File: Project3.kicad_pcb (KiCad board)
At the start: 2 copper layers, 7 parts, among them SW1 SW_Push_Open

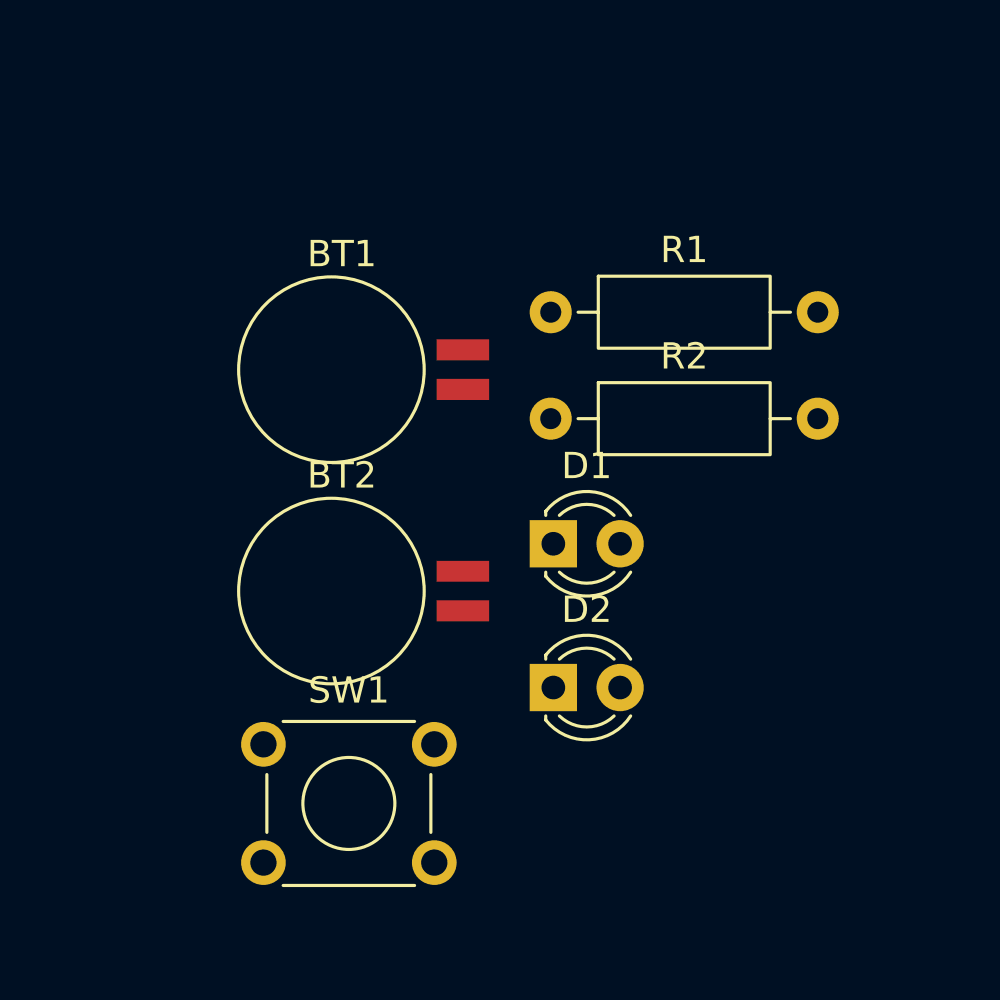
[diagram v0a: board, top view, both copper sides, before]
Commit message: Component placement is done
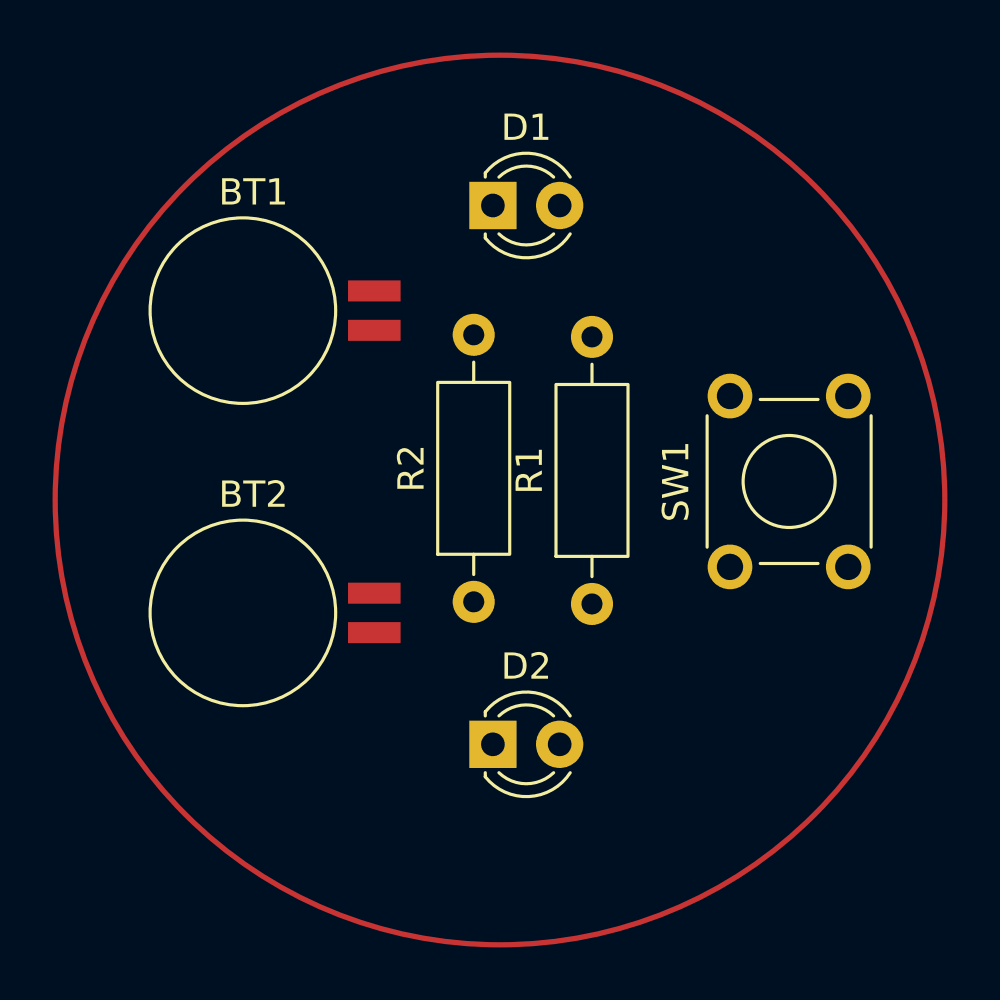
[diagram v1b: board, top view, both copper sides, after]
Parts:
- moved SW1 19.0 mm to (141.2, 85.2), turned to 90 degrees
- moved D1 13.1 mm to (132.2, 71.5)
- moved R1 11.2 mm to (136.0, 86.7), turned to 90 degrees
- moved R2 7.56 mm to (131.5, 86.6), turned to 90 degrees
- moved BT1 4.05 mm to (127.7, 75.5)
- moved BT2 3.47 mm to (127.7, 87.0)
- moved D2 3.16 mm to (132.2, 92.0)
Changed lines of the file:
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@@
 	(footprint "Resistor_THT:R_Axial_DIN0207_L6.3mm_D2.5mm_P10.16mm_Horizontal"
 		(layer "F.Cu")
-		(at 134.43 75.56)
+		(at 136 86.66 90)
 		(descr "Resistor, Axial_DIN0207 series, Axial, Horizontal, pin pitch=10.16mm, 0.25W = 1/4W, length*diameter=6.3*2.5mm^2, http://cdn-reichelt.de/documents/datenblatt/B400/1_4W%23YAG.pdf")
 		(tags "Resistor Axial_DIN0207 series Axial Horizontal pin pitch 10.16mm 0.25W = 1/4W length 6.3mm diameter 2.5mm")
 		(property "Reference" "R1"
-			(at 5.08 -2.37 0)
+			(at 5.08 -2.37 90)
 			(layer "F.SilkS")
 			(effects
@@
 		)
 		(property "Value" "R"
-			(at 5.08 2.37 0)
+			(at 5.08 2.37 90)
 			(layer "F.Fab")
 			(effects
@@
 		)
 		(property "Datasheet" "~"
-			(at 0 0 0)
+			(at 0 0 90)
 			(layer "F.Fab")
 			(hide yes)
@@
 		)
 		(property "Description" "Resistor"
-			(at 0 0 0)
+			(at 0 0 90)
 			(layer "F.Fab")
 			(hide yes)
@@
 		(attr through_hole)
 		(fp_line
+			(start 9.12 0)
+			(end 8.35 0)
+			(stroke
+				(width 0.12)
+				(type solid)
+			)
+			(layer "F.SilkS")
+		)
+		(fp_line
 			(start 1.04 0)
 			(end 1.81 0)
-			(stroke
-				(width 0.12)
-				(type solid)
-			)
-			(layer "F.SilkS")
-		)
-		(fp_line
-			(start 9.12 0)
-			(end 8.35 0)
 			(stroke
 				(width 0.12)
@@
 		)
 		(fp_line
+			(start 10.16 0)
+			(end 8.23 0)
+			(stroke
+				(width 0.1)
+				(type solid)
+			)
+			(layer "F.Fab")
+		)
+		(fp_line
 			(start 0 0)
 			(end 1.93 0)
-			(stroke
-				(width 0.1)
-				(type solid)
-			)
-			(layer "F.Fab")
-		)
-		(fp_line
-			(start 10.16 0)
-			(end 8.23 0)
 			(stroke
 				(width 0.1)
@@
 		)
 		(fp_text user "${REFERENCE}"
-			(at 5.08 0 0)
+			(at 5.08 0 90)
 			(layer "F.Fab")
 			(effects
@@
 		)
 		(pad "1" thru_hole circle
-			(at 0 0)
+			(at 0 0 90)
 			(size 1.6 1.6)
 			(drill 0.8)
@@
 		)
 		(pad "2" thru_hole circle
-			(at 10.16 0)
+			(at 10.16 0 90)
 			(size 1.6 1.6)
 			(drill 0.8)
@@
 	(footprint "Battery:BatteryHolder_Seiko_MS621F"
 		(layer "F.Cu")
-		(at 131.086204 86.168612)
+		(at 127.718102 87)
 		(descr "Seiko MS621F, https://www.sii.co.jp/en/me/files/2014/02/file_EXTENDED_PRDCT_SPEC_75_FILE_11.jpg")
 		(tags "Seiko MS621F")
 		(property "Reference" "BT2"
-			(at -4.6 -4.4 0)
+			(at -4.6 -4.5 0)
 			(layer "F.SilkS")
 			(effects
@@
 		)
 		(fp_text user "${REFERENCE}"
-			(at 0 0 0)
+			(at 0 -0.1 0)
 			(layer "F.Fab")
 			(effects
@@
 	(footprint "LED_THT:LED_D3.0mm"
 		(layer "F.Cu")
-		(at 134.53 89.84)
+		(at 132.23 92)
 		(descr "LED, diameter 3.0mm, 2 pins, generated by kicad-footprint-generator")
 		(tags "LED")
@@
 	(footprint "Battery:BatteryHolder_Seiko_MS621F"
 		(layer "F.Cu")
-		(at 131.086204 77.746204)
+		(at 127.718102 75.5)
 		(descr "Seiko MS621F, https://www.sii.co.jp/en/me/files/2014/02/file_EXTENDED_PRDCT_SPEC_75_FILE_11.jpg")
 		(tags "Seiko MS621F")
 		(property "Reference" "BT1"
-			(at -4.6 -4.4 0)
+			(at -4.6 -4.5 0)
 			(layer "F.SilkS")
 			(effects
@@
 		)
 		(fp_text user "${REFERENCE}"
-			(at 0 0 0)
+			(at 0 -0.1 0)
 			(layer "F.Fab")
 			(effects
@@
 	(footprint "LED_THT:LED_D3.0mm"
 		(layer "F.Cu")
-		(at 134.53 84.37)
+		(at 132.23 71.5)
 		(descr "LED, diameter 3.0mm, 2 pins, generated by kicad-footprint-generator")
 		(tags "LED")
@@
 		)
 		(property "Value" "LED"
-			(at 1.27 2.96 0)
+			(at 4.27 3.96 0)
 			(layer "F.Fab")
 			(effects
@@
 	(footprint "Resistor_THT:R_Axial_DIN0207_L6.3mm_D2.5mm_P10.16mm_Horizontal"
 		(layer "F.Cu")
-		(at 134.43 79.61)
+		(at 131.5 86.58 90)
 		(descr "Resistor, Axial_DIN0207 series, Axial, Horizontal, pin pitch=10.16mm, 0.25W = 1/4W, length*diameter=6.3*2.5mm^2, http://cdn-reichelt.de/documents/datenblatt/B400/1_4W%23YAG.pdf")
 		(tags "Resistor Axial_DIN0207 series Axial Horizontal pin pitch 10.16mm 0.25W = 1/4W length 6.3mm diameter 2.5mm")
 		(property "Reference" "R2"
-			(at 5.08 -2.37 0)
+			(at 5.08 -2.37 90)
 			(layer "F.SilkS")
 			(effects
@@
 		)
 		(property "Value" "R"
-			(at 5.08 2.37 0)
+			(at 5.08 2.37 90)
 			(layer "F.Fab")
 			(effects
@@
 		)
 		(property "Datasheet" "~"
-			(at 0 0 0)
+			(at 0 0 90)
 			(layer "F.Fab")
 			(hide yes)
@@
 		)
 		(property "Description" "Resistor"
-			(at 0 0 0)
+			(at 0 0 90)
 			(layer "F.Fab")
 			(hide yes)
@@
 		(attr through_hole)
 		(fp_line
+			(start 9.12 0)
+			(end 8.35 0)
+			(stroke
+				(width 0.12)
+				(type solid)
+			)
+			(layer "F.SilkS")
+		)
+		(fp_line
 			(start 1.04 0)
 			(end 1.81 0)
-			(stroke
-				(width 0.12)
-				(type solid)
-			)
-			(layer "F.SilkS")
-		)
-		(fp_line
-			(start 9.12 0)
-			(end 8.35 0)
 			(stroke
 				(width 0.12)
@@
 		)
 		(fp_line
+			(start 10.16 0)
+			(end 8.23 0)
+			(stroke
+				(width 0.1)
+				(type solid)
+			)
+			(layer "F.Fab")
+		)
+		(fp_line
 			(start 0 0)
 			(end 1.93 0)
-			(stroke
-				(width 0.1)
-				(type solid)
-			)
-			(layer "F.Fab")
-		)
-		(fp_line
-			(start 10.16 0)
-			(end 8.23 0)
 			(stroke
 				(width 0.1)
@@
 		)
 		(fp_text user "${REFERENCE}"
-			(at 5.08 0 0)
+			(at 5.08 0 90)
 			(layer "F.Fab")
 			(effects
@@
 		)
 		(pad "1" thru_hole circle
-			(at 0 0)
+			(at 0 0 90)
 			(size 1.6 1.6)
 			(drill 0.8)
@@
 		)
 		(pad "2" thru_hole circle
-			(at 10.16 0)
+			(at 10.16 0 90)
 			(size 1.6 1.6)
 			(drill 0.8)
@@
 	(footprint "Button_Switch_THT:SW_TH_Tactile_Omron_B3F-106x"
 		(layer "F.Cu")
-		(at 123.5 92)
+		(at 141.25 85.25 90)
 		(descr "Tactile switch, 6x6 mm, H7.0 mm, 6.5 mm pitch, https://omronfs.omron.com/en_US/ecb/products/pdf/en-b3f.pdf")
 		(tags "Omron B3F-10xx SPST 1P1T")
 		(property "Reference" "SW1"
-			(at 3.25 -2.05 0)
+			(at 3.25 -2.05 90)
 			(layer "F.SilkS")
 			(effects
@@
 		)
 		(property "Value" "SW_Push_Open"
-			(at 3.25 6.5 0)
+			(at 3.25 6.5 90)
 			(layer "F.Fab")
 			(effects
@@
 		)
 		(property "Datasheet" "~"
-			(at 0 0 0)
+			(at 0 0 90)
 			(unlocked yes)
 			(layer "F.Fab")
@@
 		)
 		(property "Description" "Push button switch, push-to-open, generic, two pins"
-			(at 0 0 0)
+			(at 0 0 90)
 			(unlocked yes)
 			(layer "F.Fab")
@@
 		(attr through_hole)
 		(fp_line
+			(start 0.75 -0.87)
+			(end 5.75 -0.87)
+			(stroke
+				(width 0.12)
+				(type solid)
+			)
+			(layer "F.SilkS")
+		)
+		(fp_line
+			(start 6.37 1.15)
+			(end 6.37 3.35)
+			(stroke
+				(width 0.12)
+				(type solid)
+			)
+			(layer "F.SilkS")
+		)
+		(fp_line
 			(start 0.13 3.35)
 			(end 0.13 1.15)
@@
 		)
 		(fp_line
-			(start 0.75 -0.87)
-			(end 5.75 -0.87)
-			(stroke
-				(width 0.12)
-				(type solid)
-			)
-			(layer "F.SilkS")
-		)
-		(fp_line
 			(start 0.75 5.37)
 			(end 5.75 5.37)
-			(stroke
-				(width 0.12)
-				(type solid)
-			)
-			(layer "F.SilkS")
-		)
-		(fp_line
-			(start 6.37 1.15)
-			(end 6.37 3.35)
 			(stroke
 				(width 0.12)
@@
 		(fp_line
 			(start -1.1 -1.1)
+			(end 7.6 -1.1)
+			(stroke
+				(width 0.05)
+				(type solid)
+			)
+			(layer "F.CrtYd")
+		)
+		(fp_line
+			(start -1.1 -1.1)
 			(end -1.1 5.6)
 			(stroke
@@
 		)
 		(fp_line
-			(start -1.1 -1.1)
+			(start 7.6 5.6)
 			(end 7.6 -1.1)
 			(stroke
@@
 		)
 		(fp_line
-			(start 7.6 5.6)
-			(end 7.6 -1.1)
-			(stroke
-				(width 0.05)
-				(type solid)
-			)
-			(layer "F.CrtYd")
+			(start 6.25 -0.75)
+			(end 6.25 5.25)
+			(stroke
+				(width 0.1)
+				(type solid)
+			)
+			(layer "F.Fab")
+		)
+		(fp_line
+			(start 0.25 -0.75)
+			(end 6.25 -0.75)
+			(stroke
+				(width 0.1)
+				(type solid)
+			)
+			(layer "F.Fab")
 		)
 		(fp_line
@@
 		)
 		(fp_line
-			(start 0.25 -0.75)
-			(end 6.25 -0.75)
-			(stroke
-				(width 0.1)
-				(type solid)
-			)
-			(layer "F.Fab")
-		)
-		(fp_line
 			(start 0.25 5.25)
 			(end 6.25 5.25)
@@
 			(layer "F.Fab")
 		)
-		(fp_line
-			(start 6.25 -0.75)
-			(end 6.25 5.25)
-			(stroke
-				(width 0.1)
-				(type solid)
-			)
-			(layer "F.Fab")
-		)
 		(fp_text user "${REFERENCE}"
-			(at 3.25 2.25 0)
+			(at 3.25 2.25 90)
 			(layer "F.Fab")
 			(effects
@@
 		)
 		(pad "1" thru_hole circle
-			(at 0 0)
+			(at 0 0 90)
 			(size 1.7 1.7)
 			(drill 1)
@@
 		)
 		(pad "1" thru_hole circle
-			(at 6.5 0)
+			(at 6.5 0 90)
 			(size 1.7 1.7)
 			(drill 1)
@@
 		)
 		(pad "2" thru_hole circle
-			(at 0 4.5)
+			(at 0 4.5 90)
 			(size 1.7 1.7)
 			(drill 1)
@@
 		)
 		(pad "2" thru_hole circle
-			(at 6.5 4.5)
+			(at 6.5 4.5 90)
 			(size 1.7 1.7)
 			(drill 1)
@@
 		)
 	)
+	(gr_circle
+		(center 132.5 82.704651)
+		(end 119 72.5)
+		(stroke
+			(width 0.2)
+			(type default)
+		)
+		(fill no)
+		(layer "F.Cu")
+	)
 	(embedded_fonts no)
